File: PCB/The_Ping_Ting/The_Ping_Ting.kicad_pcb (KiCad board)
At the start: 2 copper layers, 150 x 150.1 mm, 117 parts, among them J101 AudioJack2, J102 AudioJack2, J103 AudioJack2, J104 AudioJack2, J105 Jack-DC, J106 AudioJack2, J107 AudioJack2, SW201 SW_SP3T, SW301 SW_SP3T, SW401 SW_SP3T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

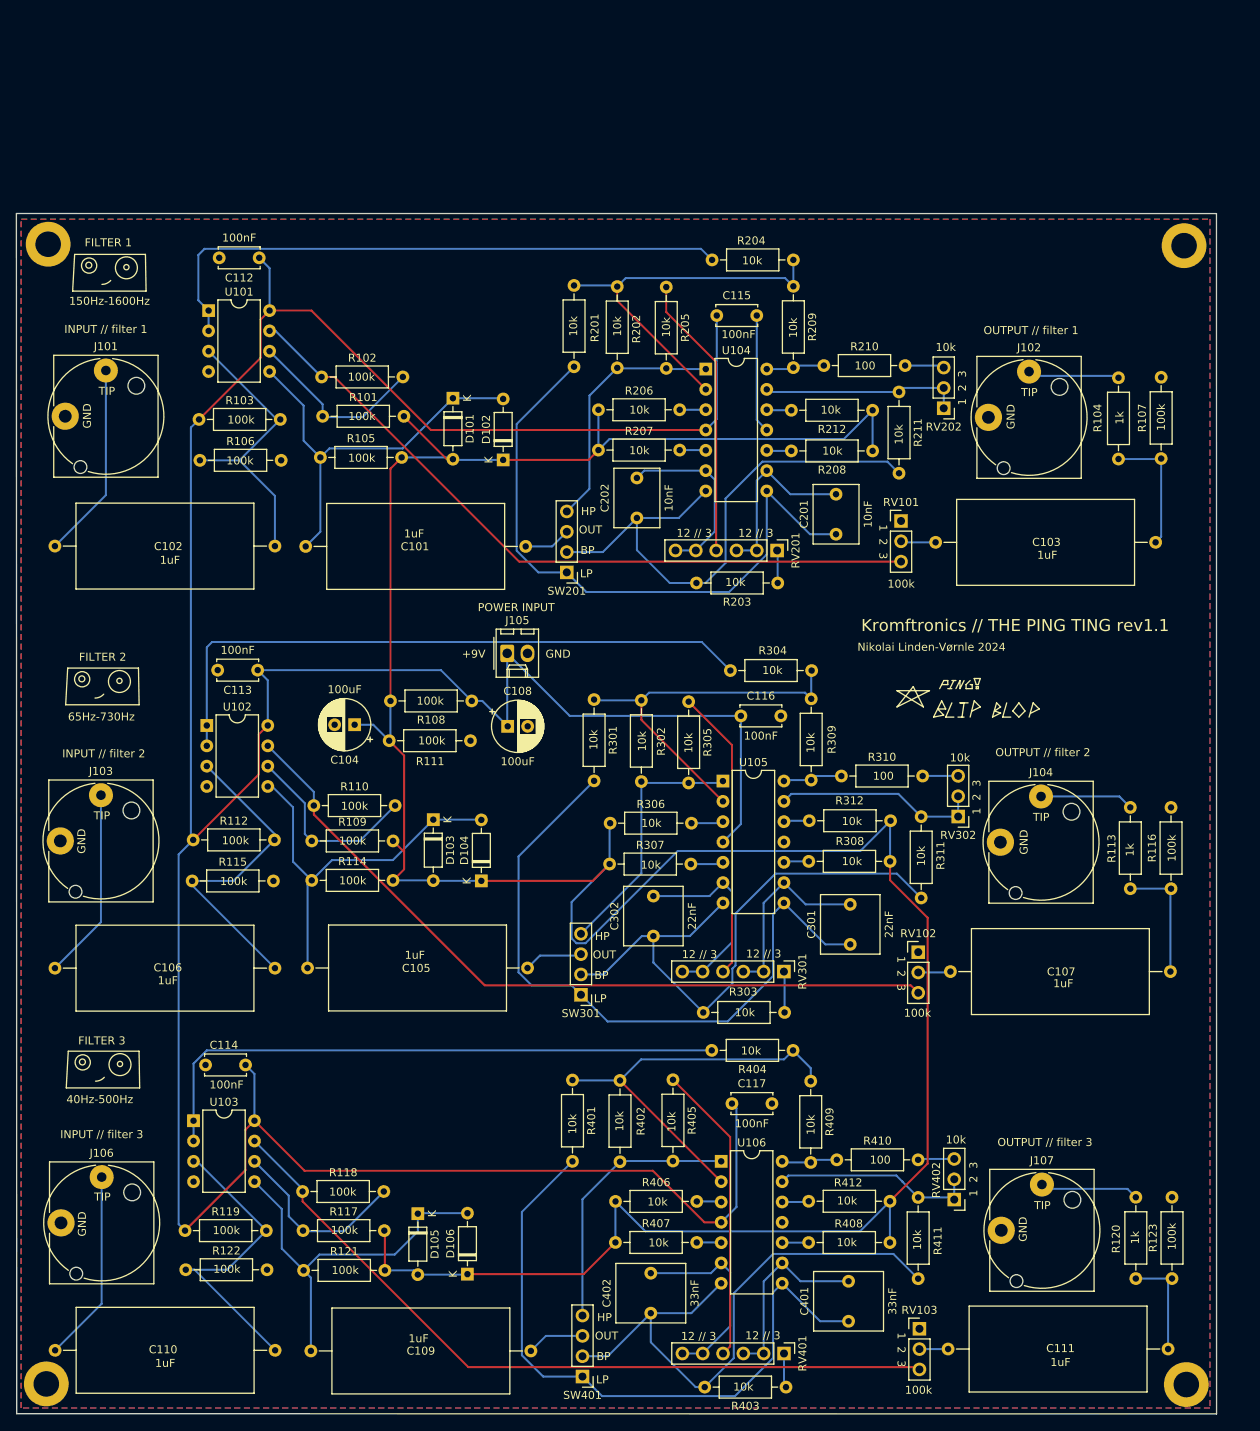
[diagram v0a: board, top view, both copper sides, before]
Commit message: added images of PCB, 3D model and schematic.
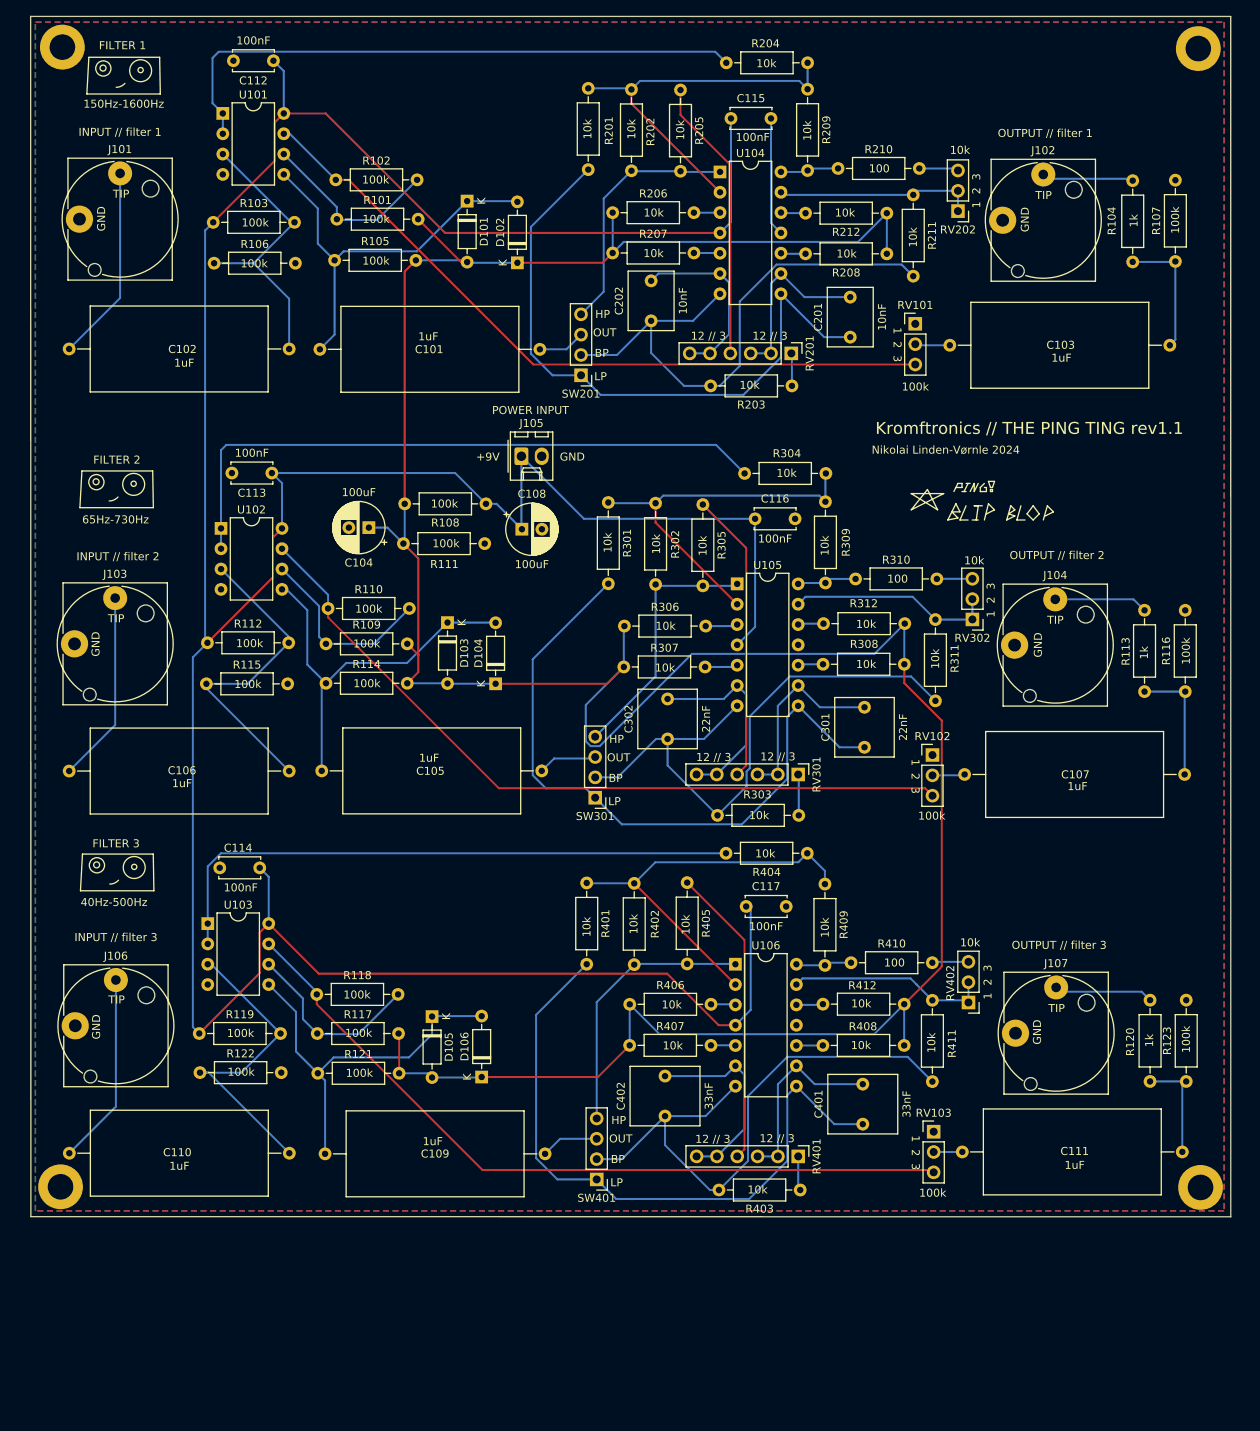
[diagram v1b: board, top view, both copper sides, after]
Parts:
- moved C301 24.7 mm to (127.0, 111.7)
- moved R114 24.7 mm to (59.7, 103.7)
- moved R404 24.7 mm to (119.8, 125.0)
- moved C106 24.7 mm to (27.6, 114.7)
- moved RV102 24.7 mm to (135.5, 112.7)
- moved C105 24.7 mm to (86.7, 114.7)
- moved C109 24.7 mm to (87.1, 162.5)
- moved C111 24.7 mm to (139.2, 162.3)
- moved D102 24.7 mm to (83.6, 51.2)
- moved J104 24.7 mm to (150.8, 93.2)
- moved R105 24.7 mm to (60.8, 50.9)
- moved R108 24.7 mm to (79.7, 81.3)
- moved R109 24.7 mm to (59.7, 98.8)
- moved R116 24.7 mm to (167.1, 104.8)
- moved R120 24.7 mm to (162.7, 143.3)
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
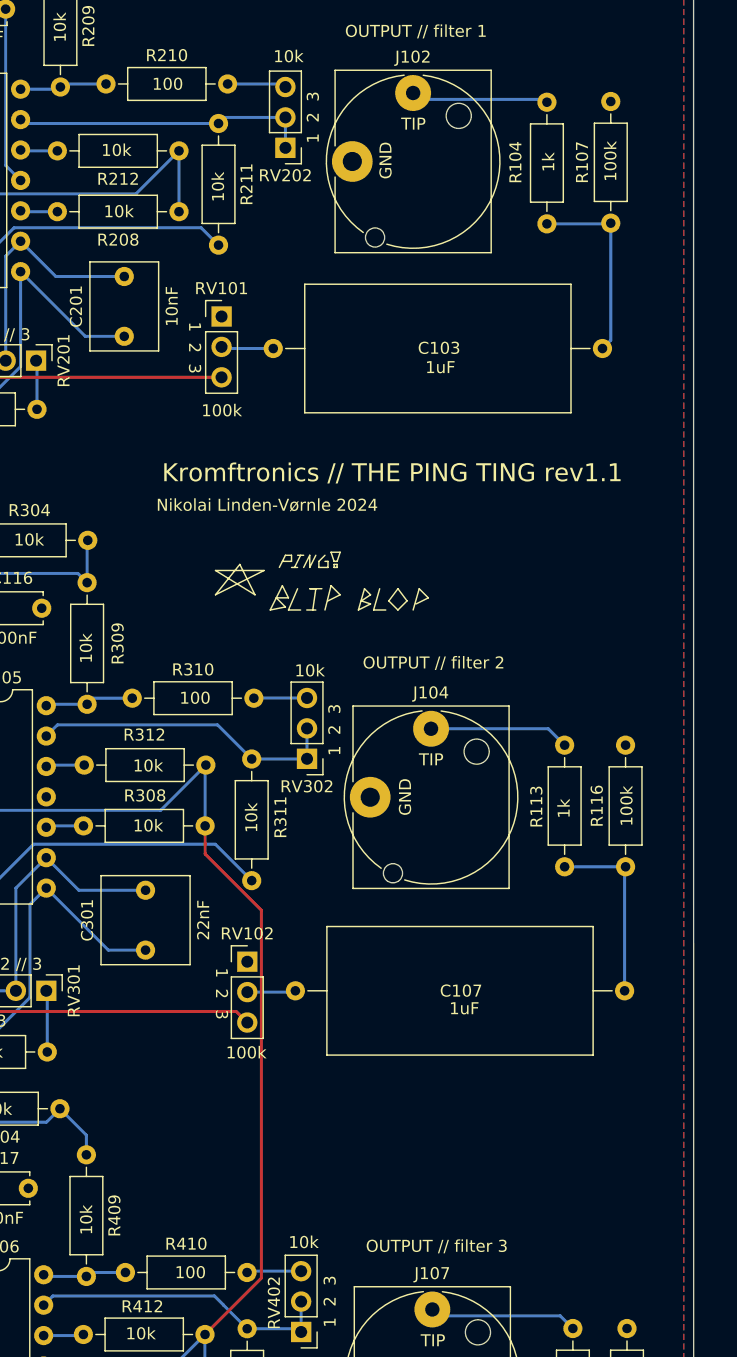
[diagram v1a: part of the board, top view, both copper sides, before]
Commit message: REVV 1.2 - Updated resonance feedback resistance Updated the feedback resistance in the mid and high frequency feedback circuit to get a more "stable" resonance level.
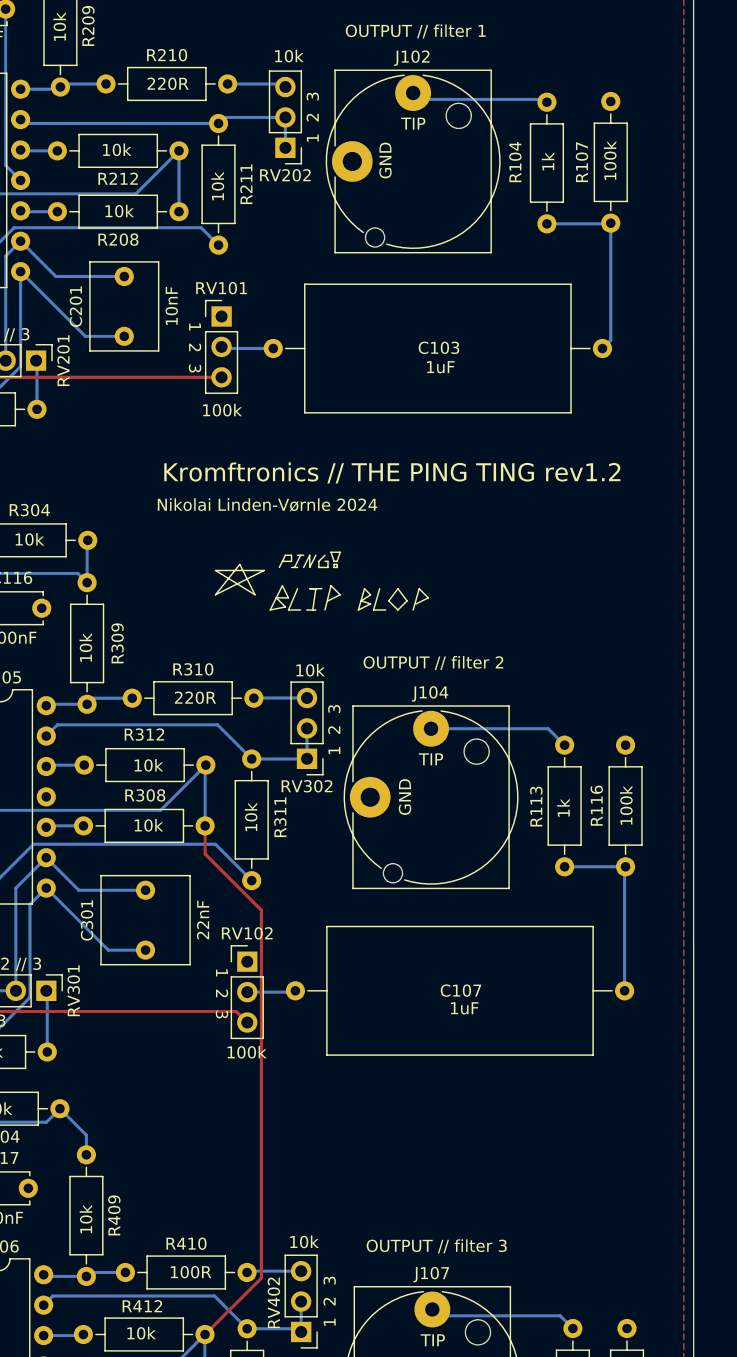
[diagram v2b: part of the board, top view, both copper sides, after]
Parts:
- R210, R310: value 100 -> 220R
- R410: value 100 -> 100R
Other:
- board text added: "Kromftronics // THE PING TING rev1.2"
- board text removed: "Kromftronics // THE PING TING rev1.1"
